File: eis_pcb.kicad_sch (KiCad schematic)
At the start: 50 parts, among them J1 Conn_01x01_Socket, J12 104031-0811, J13 10051922-1810ELF, J2 GSB1C41110SSHR, J3 Conn_01x01_Socket, J7 Conn_01x02_Socket, Q3 IRLML6344TRPBF, U1 AD5941BCPZ, U2 ESP32-S3-WROOM-1U-N16R8, U3 ESP32-S3-WROOM-1-N8R8, U4 MCP73831T-2DCI_OT, U5 NCP186AMX330TAG

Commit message: Finished PCB with manufacturing files in production folder
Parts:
- removed BOOT0, RST0: B3U-1100PM, 434121025816:434121025816, symbol Switch:SW_Push
- removed U2: ESP32-S3-WROOM-1U-N16R8, ESP32_S3_WROOM_1U_N16R8:XCVR_ESP32-S3-WROOM-1U-N16R8, symbol ESP32-S3-WROOM-1U-N16R8:ESP32-S3-WROOM-1U-N16R8
- added C25, C26: 100n, Capacitor_SMD:C_0402_1005Metric, symbol Device:C_Small
- added R17: 10k, Resistor_SMD:R_0402_1005Metric, symbol Device:R_US
- added R31: 4.7k, Resistor_SMD:R_0402_1005Metric, symbol Device:R_Small_US
- added SW1, SW2: SW_Push_Dual, SWITCH_0SMTRLFS-L:SWITCH_0SMTRLFS-L, symbol Switch:SW_Push_Dual
- added U2: LSM6DSVTR, LSM6DSVTR:LGA14-L_2P59X3P1X0P5_STM, symbol 2025-10-30_06-57-34:LSM6DSVTR
- C11, C17, C18: value 10uF -> 10u
- C12: value 100nF -> 100n
- C19, C22, C23, C24: value 1uF -> 1u
- C20: value 4.7uF -> 4.7u
- C21: value 0.1uF -> 0.1u
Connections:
- net +3V3: now also C25.1, C26.1, R17.1, R31.2, U2.8 (VDD)
- net BOOT: now also R17.2, SW2.1, SW2.2
- net CS.SCREEN: now also U3.32 (IO39); no longer U3.16 (IO46)
- net GND: now also C25.2, SW1.3, SW1.4, SW2.3, SW2.4, U2.2 (SDX), U2.3 (SCX), U2.6 (GND), U2.7 (GND)
- net MCU.RST: now also SW1.1, SW1.2
- net MISO: now also U2.1 (SDO/SA0)
- net MOSI: now also U2.14 (SDA)
- net SCLK: now also U2.13 (SCL)
- net CS.IMU: now reaches U3.26 (IO45)
- net CS.IMU: now also R31.1, U2.12 (CS)
- new net: C26.2, U2.5 (VDD_IO)
- no-connect marks 59 -> 44
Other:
- note added: "IMU"
- moved on the sheet: C11, C12, C18, C20, C21, C23, C24, J12, J13, Q3, R12, R14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

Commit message: update for multiplexed electrodes
- fix boot/reset buttons
- fix IMU
- add multiplexer
- add mezzanine electrode PCB connector
- add power path management circuit
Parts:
- removed J1, J3: Conn_01x01_Socket, Connector_Wire:SolderWirePad_1x01_SMD_1x2mm, symbol Connector:Conn_01x01_Socket
- removed J7: Conn_01x02_Socket, S2B_PH_K_S_LF__SN_:CONN_S2B-PH-K-S_JST, symbol Connector:Conn_01x02_Socket
- removed SW1, SW2: SW_Push_Dual, SWITCH_0SMTRLFS-L:SWITCH_0SMTRLFS-L, symbol Switch:SW_Push_Dual
- added C13: 0.1u, symbol Device:C_Small
- added D2: D_Schottky, symbol Device:D_Schottky
- added J4: 541020164, 541020164:CON_541020164, symbol 2026-06-17_23-18-54:541020164
- added P1: V.BATT, symbol Connector:TestPoint
- added P2: GND.BATT, symbol Connector:TestPoint
- added Q1: PMOS, symbol Simulation_SPICE:PMOS
- added R3: 100k, symbol Device:R_Small_US
- added SW1: SWT0210-045026GSA, SWT0210_045026GSA:SW_SWT0210-045026GSA_REVA, symbol SWT0210-045026GSA_REVA:SWT0210-045026GSA_REVA
- added SW2: SWT0210-045026GSA_REVA, SWT0210_045026GSA:SW_SWT0210-045026GSA_REVA, symbol SWT0210-045026GSA_REVA:SWT0210-045026GSA_REVA
- added U6: TMUX1109RSVR, TMUX1109RSVR:RSV16_TEX, symbol TMUX1109RSVR:TMUX1109RSVR
- U3: DESCRIPTION Bluetooth, WiFi 802.11b/g/n, Bluetooth v5.0 Transceiver Mod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 -> (none)
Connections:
- net +3V3: now also U2.5 (VDD_IO), C13.1, U6.12 (VDD)
- net +5V: now also D2.2 (A), Q1.2 (G), R3.2
- net +BATT: now also P1.1, Q1.1 (D); no longer C22.1, U5.6 (EN), U5.7 (IN), U5.8 (IN__1)
- net BOOT: now also SW2.1, SW2.2
- net GND: now also C26.2, C13.2, J4.1, J4.10, J4.11, J4.14, J4.3, J4.6, J4.9, P2.1, R3.1, SW1.3, SW1.4, SW2.3, SW2.4, U6.1 (VSS), U6.13 (GND)
- net MCU.RST: now also SW1.1, SW1.2
- net RE renamed CE0
- net CE0: now also U6.6 (DA); no longer U1.48 (RE0)
- net WE renamed WE0
- net WE0: now also U6.7 (DB)
- new net A0.MUX: U6.15 (A0)
- new net A1.MUX: U6.14 (A1)
- new net CE1: J4.7, U6.2 (S1A)
- new net CE2: J4.8, U6.3 (S2A)
- new net CE3: J4.15, U6.4 (S3A)
- new net CE4: J4.16, U6.5 (S4A)
- new net EN.MUX: U6.16 (EN)
- new net RE0: J4.2, U1.48 (RE0)
- new net VBUS: C22.1, D2.1 (K), Q1.3 (S), U5.6 (EN), U5.7 (IN), U5.8 (IN__1)
- new net WE1: J4.4, U6.11 (S1B)
- new net WE2: J4.5, U6.10 (S2B)
- new net WE3: J4.12, U6.9 (S3B)
- new net WE4: J4.13, U6.8 (S4B)
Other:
- note added: "3.7V LiPo Solder Pads"
- note added: "AFE"
- note added: "Electrode Connector"
- note added: "Electrode Multiplexer"
- note added: "Power Path Management"
- note removed: "3.7V LiPo Connector"
- note removed: "EIS IC"
- note removed: "Electrodes"
- moved on the sheet: C1, C10, C11, C12, C17, C18, C19, C2, C20, C21, C22, C23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

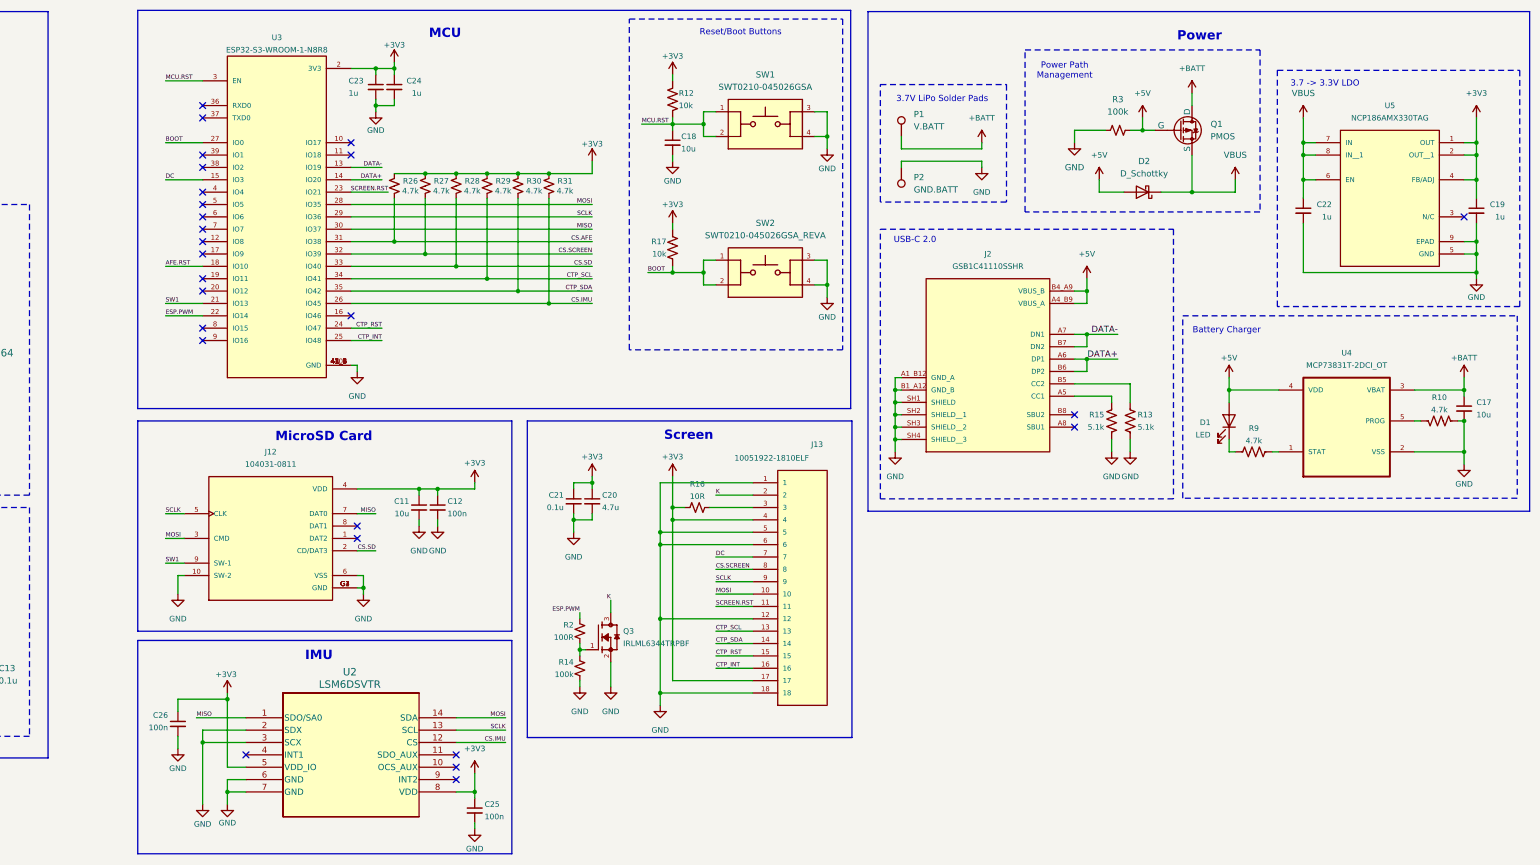
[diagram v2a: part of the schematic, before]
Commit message: update power circuit
- switch to BQ24075 charge controller with integrated DPPM
- add 2.8V LDO for display
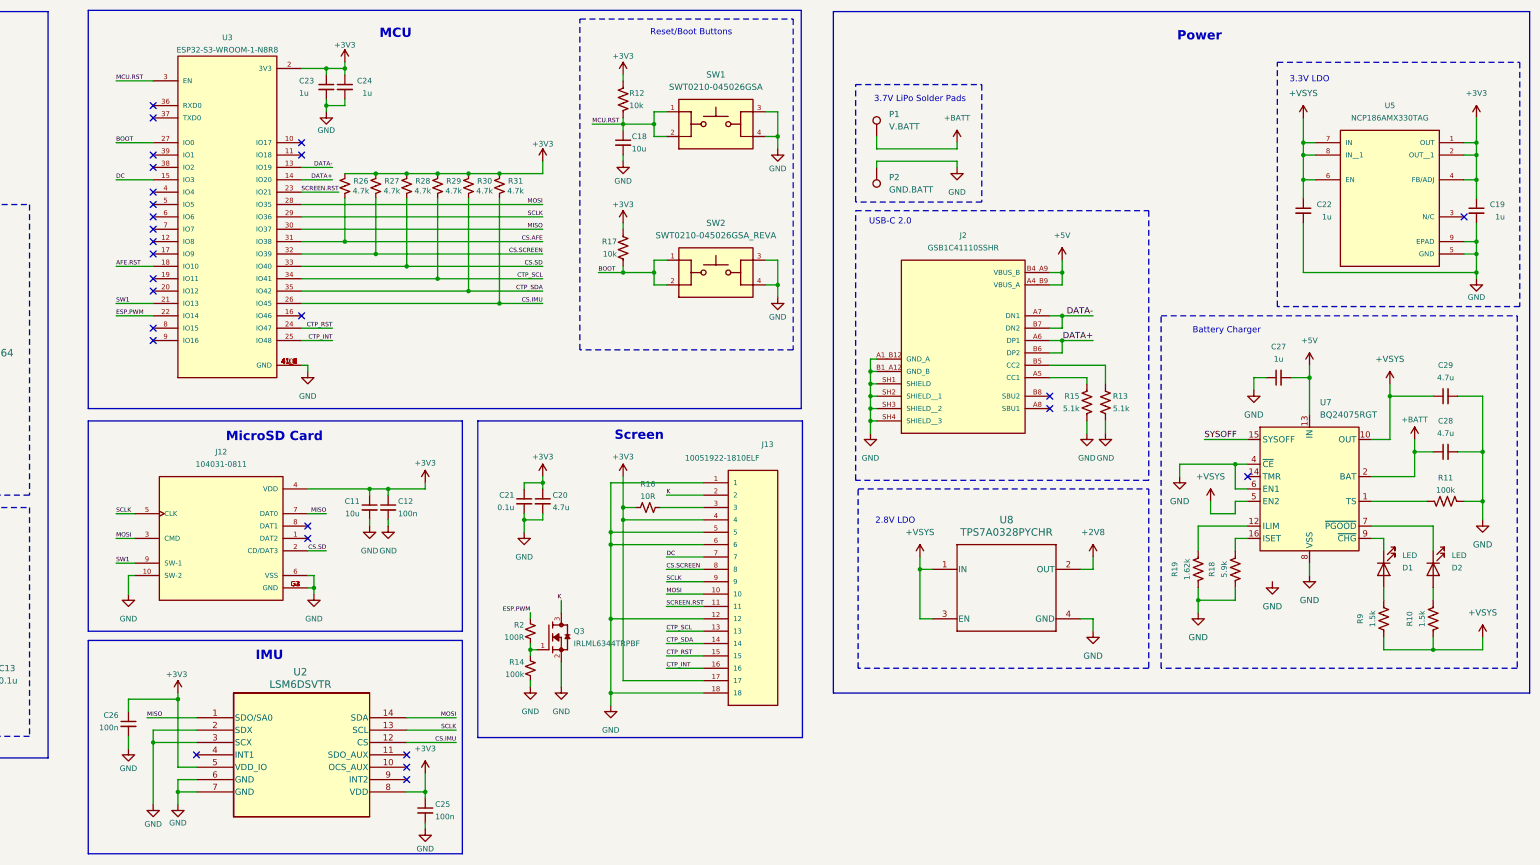
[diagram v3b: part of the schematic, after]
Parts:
- removed C17: 10u, Capacitor_SMD:C_0603_1608Metric, symbol Device:C_Small
- removed D2: D_Schottky, symbol Device:D_Schottky
- removed Q1: PMOS, symbol Simulation_SPICE:PMOS
- removed R3: 100k, symbol Device:R_Small_US
- removed U4: MCP73831T-2DCI_OT, MCP73831T-2DCI_OT:SOT95P270X145-5N, symbol MCP73831T-2DCI_OT:MCP73831T-2DCI_OT
- added C27: 1u, Capacitor_SMD:C_0603_1608Metric, symbol Device:C_Small
- added C28, C29: 4.7u, Capacitor_SMD:C_0603_1608Metric, symbol Device:C_Small
- added D2: LED, LED_SMD:LED_0603_1608Metric, symbol Device:LED
- added R11: 100k, Resistor_SMD:R_0402_1005Metric, symbol Device:R_US
- added R18: 5.9k, Resistor_SMD:R_0402_1005Metric, symbol Device:R_US
- added R19: 1.62k, Resistor_SMD:R_0402_1005Metric, symbol Device:R_US
- added U7: BQ24075RGT, Package_DFN_QFN:VQFN-16-1EP_3x3mm_P0.5mm_EP1.6x1.6mm, symbol Battery_Management:BQ24075RGT
- added U8: TPS7A0328PYCHR, YCH0004-IPC_A, symbol 2026-06-18_22-09-09:TPS7A0328PYCHR
- R10, R9: value 4.7k -> 1.5k
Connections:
- net VBUS is gone; now on net +VSYS: C22.1, U5.6 (EN), U5.7 (IN), U5.8 (IN__1)
- net +5V: now also C27.2, U7.13 (IN); no longer D1.2 (A)
- net +BATT: now also C28.1, U7.2 (BAT), U7.3 (BAT)
- net GND: now also C27.1, C28.2, C29.2, R11.1, R18.2, R19.2, U7.17 (VSS), U7.4 (~{CE}), U7.6 (EN1), U7.8 (VSS), U8.4 (GND); no longer R10.1
- net +VSYS: now reaches R10.2
- net +VSYS: now also R9.1, C29.1, U7.10 (OUT), U7.11 (OUT), U7.5 (EN2), U8.1 (IN), U8.3 (EN)
- net at D1.1 (K): now also U7.9 (~{CHG}); no longer R9.1
- net at R9.2: now also D1.2 (A)
- new net: R11.2, U7.1 (TS)
- new net: R19.1, U7.12 (ILIM)
- new net: R18.1, U7.16 (ISET)
- new net: D2.1 (K), U7.7 (~{PGOOD})
- new net: D2.2 (A), R10.1
- new net +2V8: U8.2 (OUT)
- new net SYSOFF: U7.15 (SYSOFF)
- no-connect marks 44 -> 45
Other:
- note added: "2.8V LDO"
- note added: "3.3V LDO"
- note removed: "3.7 -> 3.3V LDO"
- note removed: "Power Path Management"
- moved on the sheet: C11, C12, C18, C20, C21, C23, C24, C25, C26, D1, J12, J13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
